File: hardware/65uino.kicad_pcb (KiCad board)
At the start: 2 copper layers, 75.4 x 53.6 mm, 42 parts, among them J1 Barrel_Jack_MountingPin, J2 USB_B_Micro, J3 OLED, SW1 RST, SW2 BTN, U1 R6507, U2 74HC04, U3 6532, U4 w27C512, U5 MIC5504-3.3YM5, U6 LM1117-5.0, Y1 1Mhz

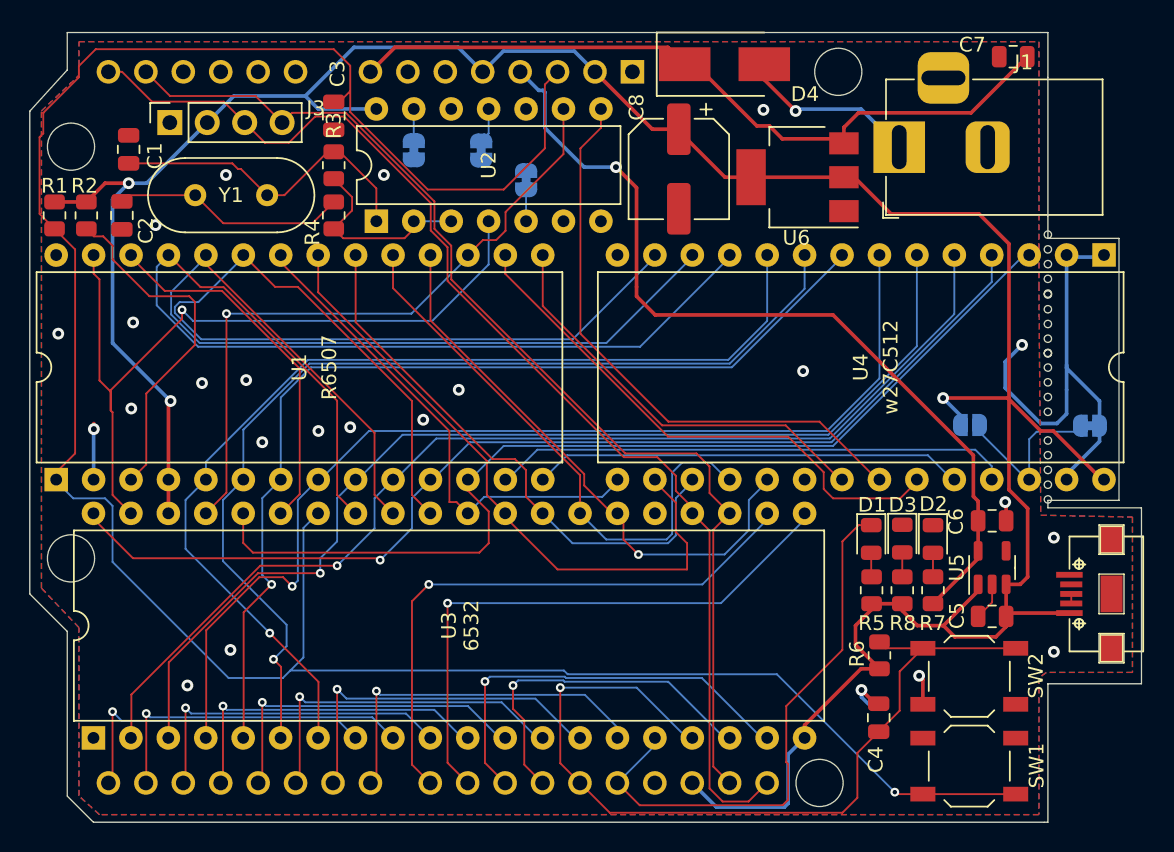
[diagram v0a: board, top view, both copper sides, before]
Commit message: Gerbers and SMD osc. added
First batch of PCB's ordered. Pads for an SMD oscillator added + extra decoupling pads.
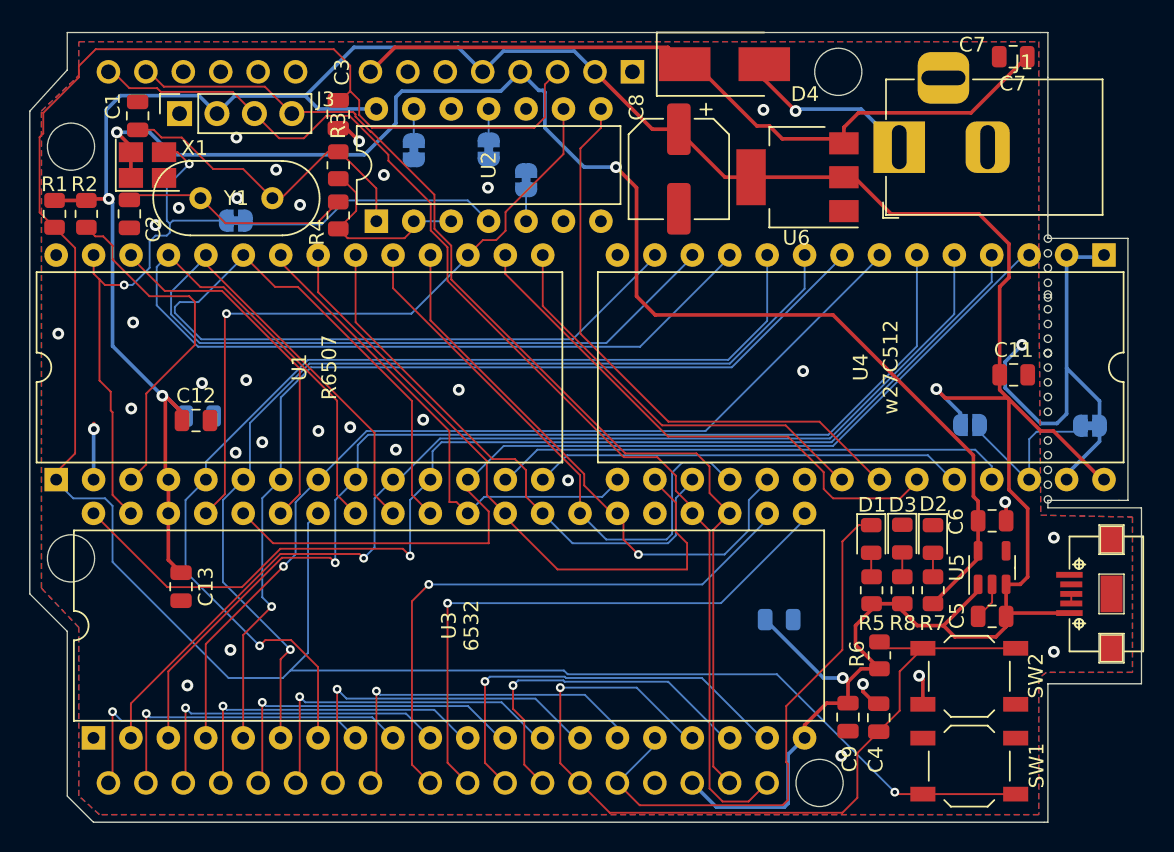
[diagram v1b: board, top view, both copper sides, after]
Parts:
- added C10: NC, Capacitor_SMD:C_0805_2012Metric, B.Cu at (113.2, 74.4)
- added C11: 100nF, Capacitor_SMD:C_0805_2012Metric, F.Cu at (168.5, 71.6)
- added C12: 100nF, Capacitor_SMD:C_0805_2012Metric, F.Cu at (113.0, 74.7)
- added C13: 100nF, Capacitor_SMD:C_0805_2012Metric, F.Cu at (112.0, 86.0)
- added C14: NC, Capacitor_SMD:C_0805_2012Metric, B.Cu at (152.6, 88.2)
- added C9: 100nF, Capacitor_SMD:C_0805_2012Metric, F.Cu at (157.2, 94.9)
- added JP6: SolderJumper_2_Bridged, Jumper:SolderJumper-2_P1.3mm_Bridged_RoundedPad1.0x1.5mm, B.Cu at (115.7, 61.2)
- added X1: NC, Oscillator:Oscillator_SMD_SeikoEpson_SG210-4Pin_2.5x2.0mm_HandSoldering, F.Cu at (109.7, 57.4)
- moved C1 2.36 mm to (109.0, 54.1)
- moved J3 0.90 mm to (111.9, 53.9)
- moved C2 0.52 mm to (108.5, 60.7)
- moved JP5 0.51 mm to (132.8, 56.3)
- moved Y1 0.41 mm to (118.2, 59.6)
- moved C3 0.32 mm to (122.6, 53.9)
- moved R3 0.30 mm to (122.6, 57.4)
- moved R4 0.30 mm to (122.6, 60.8)
- moved REF** 0.27 mm to (170.8, 62.4)
- moved R1 0.10 mm to (103.4, 60.7)
- moved R2 0.10 mm to (105.5, 60.7)
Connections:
- U2 pad 4: Net-(U1-Pad27) -> Net-(U2-Pad4)
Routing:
- net +3V3: track 58.7 -> 92.7 mm, vias 1 -> 2
- net +5V: track 192.9 -> 213.1 mm, vias 3 -> 4
- net Net-(U2-Pad4): track 0.00 -> 17.5 mm
- net Net-(U1-Pad27): track 53.0 -> 37.4 mm, vias 1 -> 2
- net A3: track 72.0 -> 64.8 mm
- net Net-(A1-Pad3): track 164.8 -> 158.9 mm
- net A6: track 73.2 -> 76.9 mm
- net A7: track 68.8 -> 66.1 mm
- net A0: track 69.4 -> 71.2 mm
- net Net-(JP1-Pad2): track 12.3 -> 10.9 mm
- net A4: track 73.2 -> 74.5 mm
- net Net-(A1-Pad22): track 24.5 -> 23.2 mm
- net Net-(A1-Pad8): track 51.0 -> 49.9 mm
- net Net-(A1-Pad27): track 58.9 -> 57.9 mm
- net Net-(R3-Pad1): track 13.5 -> 12.5 mm
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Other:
- outline, holes or cut-outs redrawn
